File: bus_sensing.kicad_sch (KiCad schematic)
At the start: 2 parts

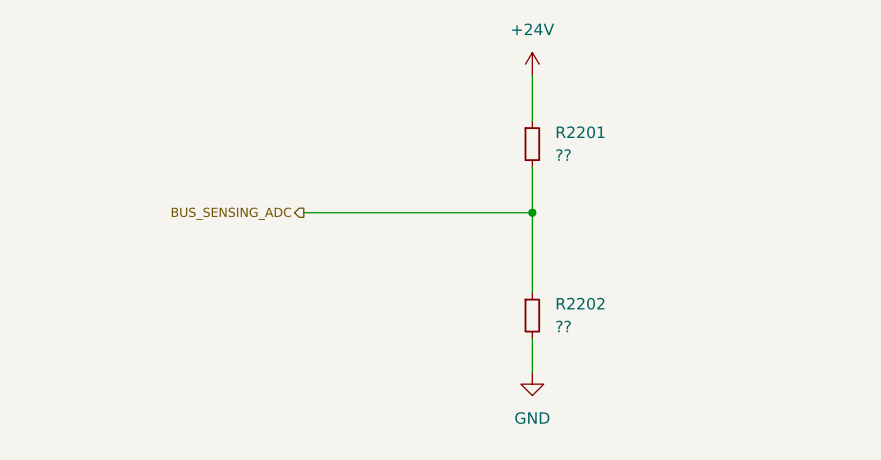
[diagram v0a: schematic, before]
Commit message: Add power stages
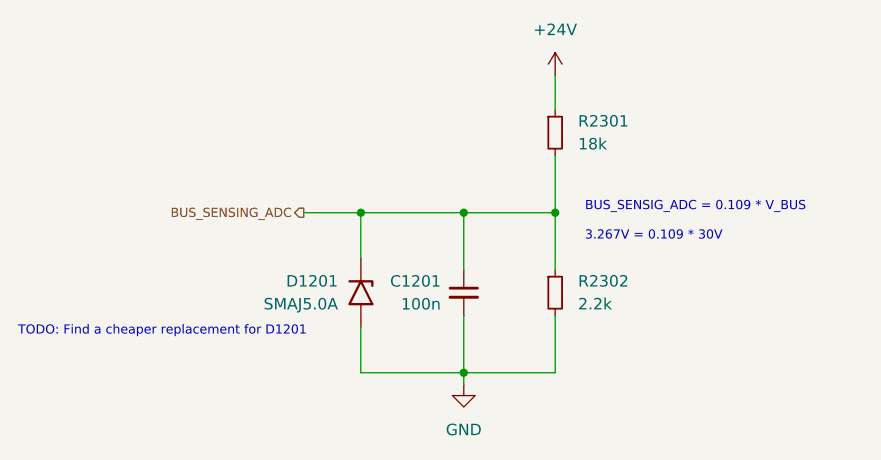
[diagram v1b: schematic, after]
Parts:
- added C1201: 100n, symbol Device:C_Small
- added D1201: SMAJ5.0A, Diode_SMD:D_SMA, symbol Diode:SMAJ5.0A
- R2301: renamed from R2201; value ?? -> 18k
- R2302: renamed from R2202; value ?? -> 2.2k
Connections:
- net BUS_SENSING_ADC: now also C1201.1, D1201.1 (A1)
- net GND: now also C1201.2, D1201.2 (A2)
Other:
- note added: "BUS_SENSIG_ADC = 0.109 * V_BUS 3.267V = 0.109 * 30V"
- note added: "TODO: Find a cheaper replacement for D1201"
- moved on the sheet: R2301, R2302
